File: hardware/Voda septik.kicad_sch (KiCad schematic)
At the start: 39 parts, among them J1 Screw_Terminal_01x09, J2 RS-485 elektroměr, J3 Display TM1637, J4 Display LCD I2C, U1 ESP32-DevKitC-30, U2 DC-DC 24V -> 5V, U4 MAX3485-modul

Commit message: Doladění průtoku a schematu.
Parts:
- removed R10: 22k, symbol Device:R
- removed R12: 10k, symbol Device:R
- added C6: 100p, symbol Device:C
- added C7: 1n, symbol Device:C
- C3: value 100n -> 15n
- D5: value ~ -> 1N4007; footprint (none) -> Diode_THT:D_DO-41_SOD81_P10.16mm_Horizontal
- R1: value 10k -> 2k2
- R11: value 10k -> 56R
- R2: value 10k -> 3k9
- R4: value 2k2 -> 2k7
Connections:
- net GND: now also C6.2, C7.2
- net průtok_MCU: now also R2.2, C7.1
- net temp_MCU: now also C6.1
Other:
- moved on the sheet: R2

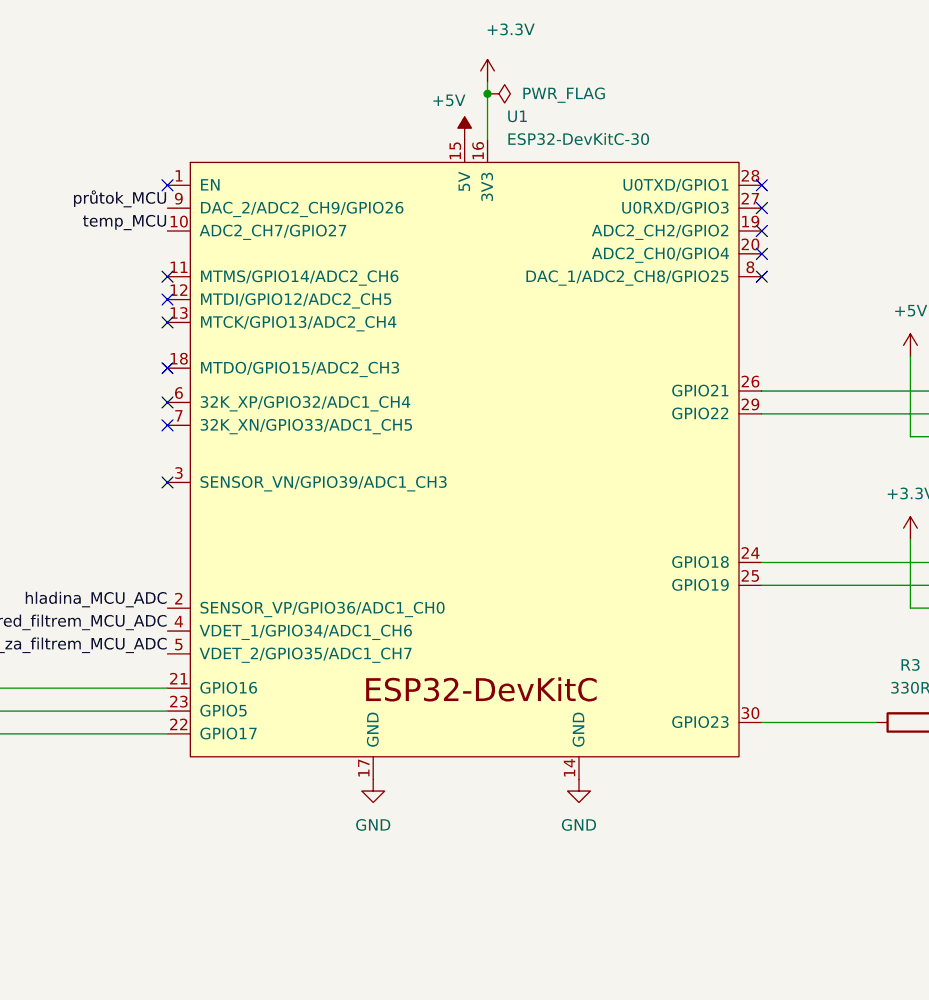
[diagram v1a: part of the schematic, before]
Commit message: Upravit schéma podle skutečnosti.
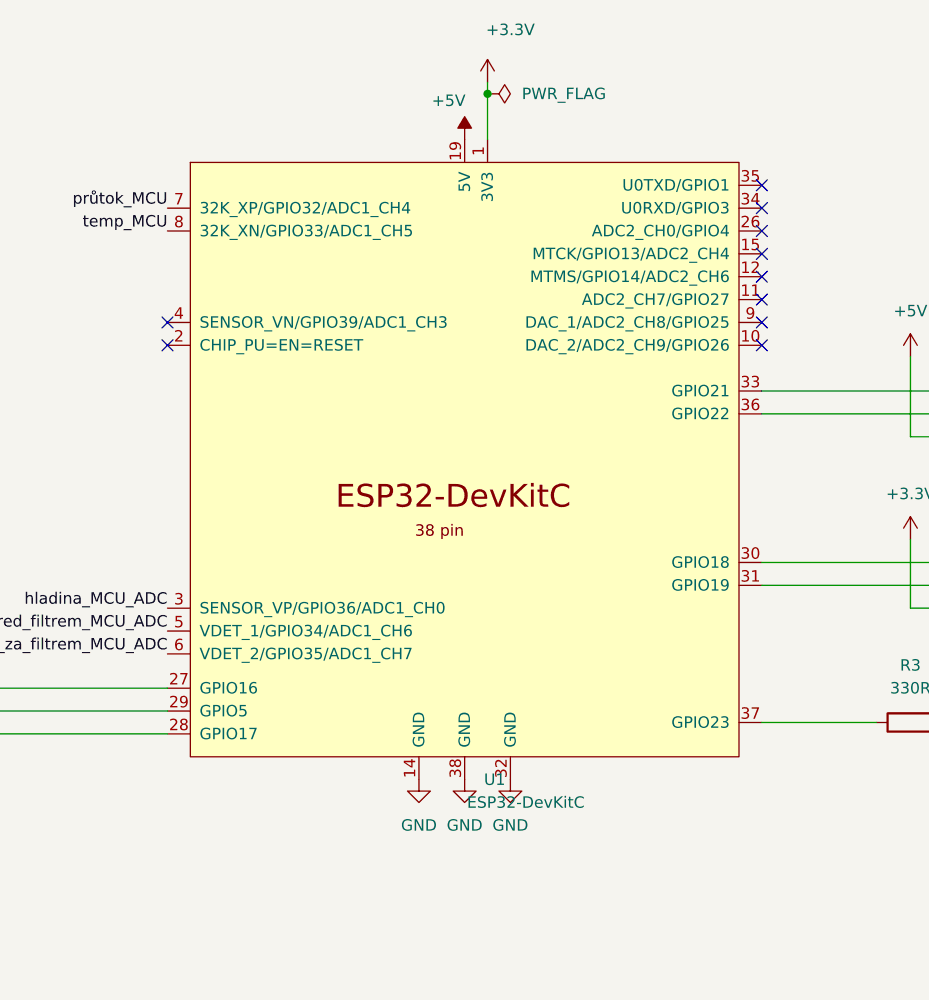
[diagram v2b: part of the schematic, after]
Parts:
- U1: value ESP32-DevKitC-30 -> ESP32-DevKitC; footprint martin:ESP32-DevKitC-30 -> PCM_Espressif:ESP32-DevKitC; symbol martin:ESP32-DevKitC-30 -> PCM_Espressif:ESP32-DevKitC
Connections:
- net +3.3V: now also U1.1 (3V3); no longer U1.16 (3V3)
- net +5V: now also U1.19 (5V); no longer U1.15 (5V)
- net GND: now also U1.32 (GND), U1.38 (GND); no longer U1.17 (GND)
- net hladina_MCU_ADC: now also U1.3 (SENSOR_VP/GPIO36/ADC1_CH0); no longer U1.2 (SENSOR_VP/GPIO36/ADC1_CH0)
- net průtok_MCU: now also U1.7 (32K_XP/GPIO32/ADC1_CH4); no longer U1.9 (DAC_2/ADC2_CH9/GPIO26)
- net temp_MCU: now also U1.8 (32K_XN/GPIO33/ADC1_CH5); no longer U1.10 (ADC2_CH7/GPIO27)
- net tlak_pred_filtrem_MCU_ADC: now also U1.5 (VDET_1/GPIO34/ADC1_CH6); no longer U1.4 (VDET_1/GPIO34/ADC1_CH6)
- net tlak_za_filtrem_MCU_ADC: now also U1.6 (VDET_2/GPIO35/ADC1_CH7); no longer U1.5 (VDET_2/GPIO35/ADC1_CH7)
- net at R3.1: now also U1.37 (GPIO23); no longer U1.30 (GPIO23)
- net at J3.3 (DIO): now also U1.31 (GPIO19); no longer U1.25 (GPIO19)
- net at J3.4 (CLK): now also U1.30 (GPIO18); no longer U1.24 (GPIO18)
- net at U4.1 (RXD): now also U1.27 (GPIO16); no longer U1.21 (GPIO16)
- net at U4.3 (EN): now also U1.29 (GPIO5); no longer U1.23 (GPIO5)
- net at U4.4 (TXD): now also U1.28 (GPIO17); no longer U1.22 (GPIO17)
- net at U1.26 (ADC2_CH0/GPIO4): no longer J4.4 (SCL)
- net at J4.3 (SDA): now also U1.36 (GPIO22); no longer U1.29 (GPIO22)
- new net: J4.4 (SCL), U1.33 (GPIO21)
- no-connect marks 13 -> 10
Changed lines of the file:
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@@
 	)
 	(no_connect
-		(at 165.1 40.64)
+		(at 231.14 45.72)
 	)
 	(no_connect
@@
 	)
 	(no_connect
-		(at 165.1 43.18)
+		(at 231.14 48.26)
 	)
 	(no_connect
-		(at 165.1 30.48)
+		(at 231.14 43.18)
 	)
 	(no_connect
@@
 	)
 	(no_connect
-		(at 165.1 57.15)
-	)
-	(no_connect
 		(at 231.14 30.48)
 	)
 	(no_connect
-		(at 165.1 54.61)
-	)
-	(no_connect
-		(at 165.1 63.5)
-	)
-	(no_connect
 		(at 231.14 40.64)
 	)
 	(no_connect
-		(at 165.1 50.8)
+		(at 165.1 48.26)
 	)
 	(wire
@@
 	(symbol
 		(lib_id "power:GND")
-		(at 210.82 96.52 0)
+		(at 203.2 96.52 0)
 		(unit 1)
 		(exclude_from_sim no)
@@
 		(fields_autoplaced yes)
 		(property "Reference" "#PWR021"
-			(at 210.82 102.87 0)
+			(at 203.2 102.87 0)
 			(effects
 				(font
@@
 		)
 		(property "Value" "GND"
-			(at 210.82 101.6 0)
+			(at 203.2 101.6 0)
 			(effects
 				(font
@@
 		)
 		(property "Footprint" ""
-			(at 210.82 96.52 0)
+			(at 203.2 96.52 0)
 			(effects
 				(font
@@
 		)
 		(property "Datasheet" ""
-			(at 210.82 96.52 0)
+			(at 203.2 96.52 0)
 			(effects
 				(font
@@
 		)
 		(property "Description" "Power symbol creates a global label with name \"GND\" , ground"
-			(at 210.82 96.52 0)
+			(at 203.2 96.52 0)
 			(effects
 				(font
@@
 	)
 	(symbol
-		(lib_id "martin:ESP32-DevKitC-30")
+		(lib_id "PCM_Espressif:ESP32-DevKitC")
 		(at 198.12 60.96 0)
 		(unit 1)
@@
 		(on_board yes)
 		(dnp no)
-		(fields_autoplaced yes)
 		(property "Reference" "U1"
-			(at 202.8033 22.86 0)
+			(at 200.2633 96.52 0)
 			(effects
 				(font
@@
 			)
 		)
-		(property "Value" "ESP32-DevKitC-30"
-			(at 202.8033 25.4 0)
+		(property "Value" "ESP32-DevKitC"
+			(at 198.374 99.06 0)
 			(effects
 				(font
@@
 			)
 		)
-		(property "Footprint" "martin:ESP32-DevKitC-30"
+		(property "Footprint" "PCM_Espressif:ESP32-DevKitC"
 			(at 198.12 104.14 0)
 			(effects
@@
 		(pin "22"
 		)
+		(pin "32"
+		)
+		(pin "38"
+		)
+		(pin "35"
+		)
+		(pin "34"
+		)
+		(pin "31"
+		)
+		(pin "33"
+		)
+		(pin "36"
+		)
+		(pin "37"
+		)
 		(instances
 			(project ""
@@
 	)
 	(symbol
+		(lib_id "power:GND")
+		(at 198.12 96.52 0)
+		(unit 1)
+		(exclude_from_sim no)
+		(in_bom yes)
+		(on_board yes)
+		(dnp no)
+		(fields_autoplaced yes)
+		(property "Reference" "#PWR026"
+			(at 198.12 102.87 0)
+			(effects
+				(font
+					(size 1.27 1.27)
+				)
+				(hide yes)
+			)
+		)
+		(property "Value" "GND"
+			(at 198.12 101.6 0)
+			(effects
+				(font
+					(size 1.27 1.27)
+				)
+			)
+		)
+		(property "Footprint" ""
+			(at 198.12 96.52 0)
+			(effects
+				(font
+					(size 1.27 1.27)
+				)
+				(hide yes)
+			)
+		)
+		(property "Datasheet" ""
+			(at 198.12 96.52 0)
+			(effects
+				(font
+					(size 1.27 1.27)
+				)
+				(hide yes)
+			)
+		)
+		(property "Description" "Power symbol creates a global label with name \"GND\" , ground"
+			(at 198.12 96.52 0)
+			(effects
+				(font
+					(size 1.27 1.27)
+				)
+				(hide yes)
+			)
+		)
+		(pin "1"
+		)
+		(instances
+			(project "Voda septik"
+				(path "/cbe5bfb0-423d-4741-99d1-40044a77c19e"
+					(reference "#PWR026")
+					(unit 1)
+				)
+			)
+		)
+	)
+	(symbol
 		(lib_id "martin:DC_DC_LM2596_HW411")
 		(at 57.15 27.94 0)
@@
 	(symbol
 		(lib_id "power:GND")
-		(at 187.96 96.52 0)
+		(at 193.04 96.52 0)
 		(unit 1)
 		(exclude_from_sim no)
@@
 		(fields_autoplaced yes)
 		(property "Reference" "#PWR020"
-			(at 187.96 102.87 0)
+			(at 193.04 102.87 0)
 			(effects
 				(font
@@
 		)
 		(property "Value" "GND"
-			(at 187.96 101.6 0)
+			(at 193.04 101.6 0)
 			(effects
 				(font
@@
 		)
 		(property "Footprint" ""
-			(at 187.96 96.52 0)
+			(at 193.04 96.52 0)
 			(effects
 				(font
@@
 		)
 		(property "Datasheet" ""
-			(at 187.96 96.52 0)
+			(at 193.04 96.52 0)
 			(effects
 				(font
@@
 		)
 		(property "Description" "Power symbol creates a global label with name \"GND\" , ground"
-			(at 187.96 96.52 0)
+			(at 193.04 96.52 0)
 			(effects
 				(font

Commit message: Úprava schématu, asi popisky.
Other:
- note added: "hladina"
- note added: "průtok"
- note added: "svítí při chybě senzoru"
- note added: "teplota voda"
- note added: "teplota vzduch"
- note added: "tlak před filtrem"
- note added: "tlak za filtrem"

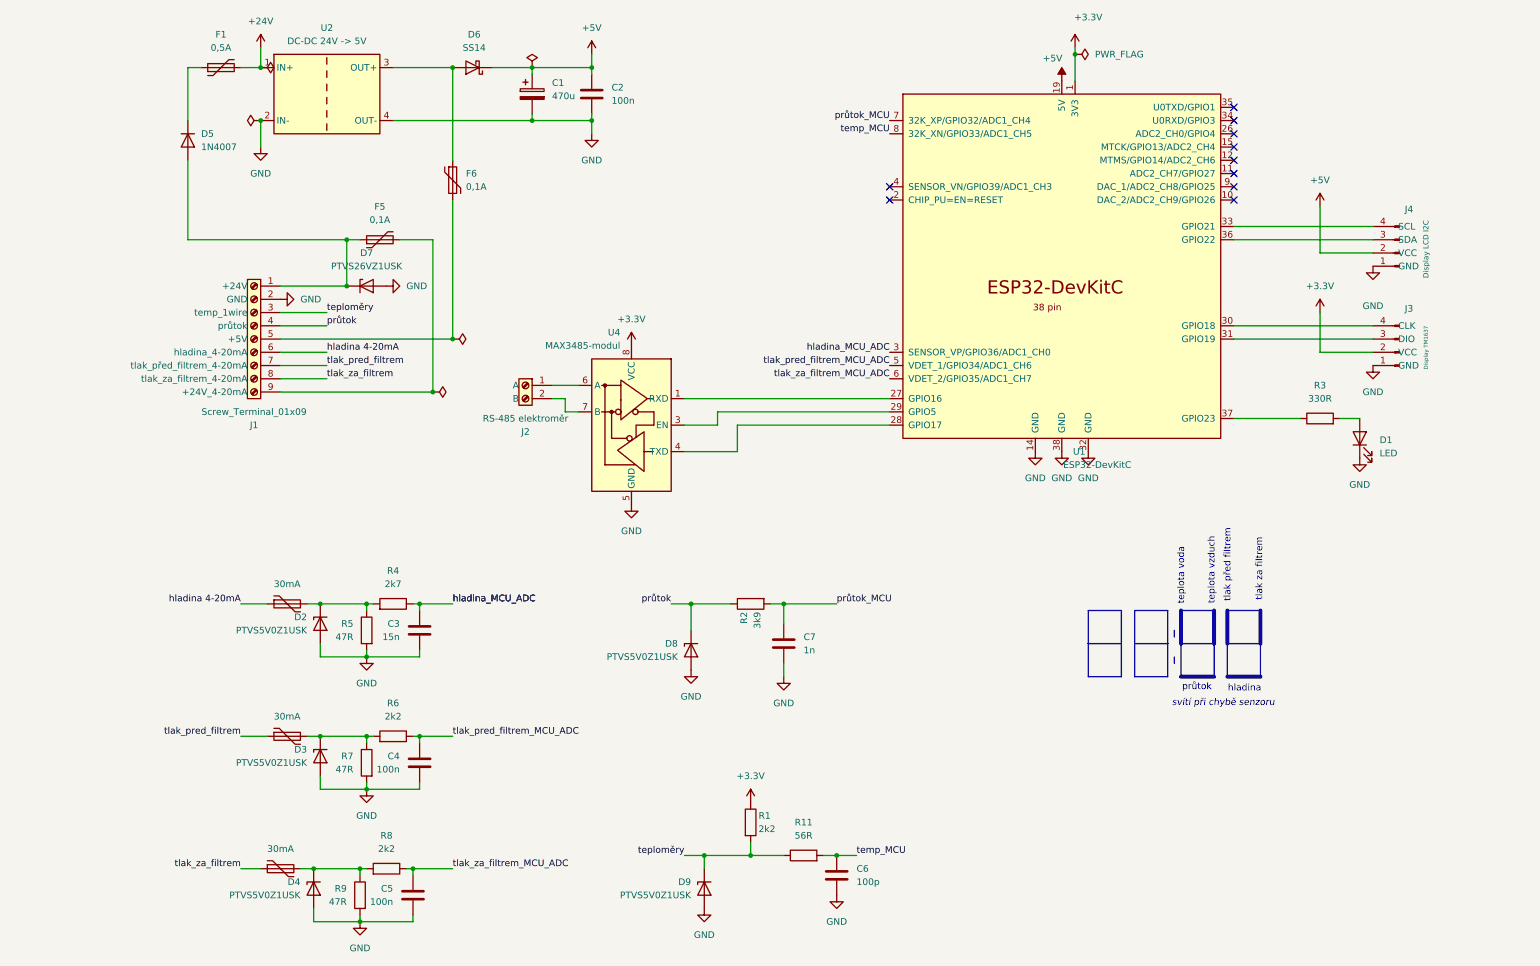
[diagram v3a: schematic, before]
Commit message: Úprava schématu
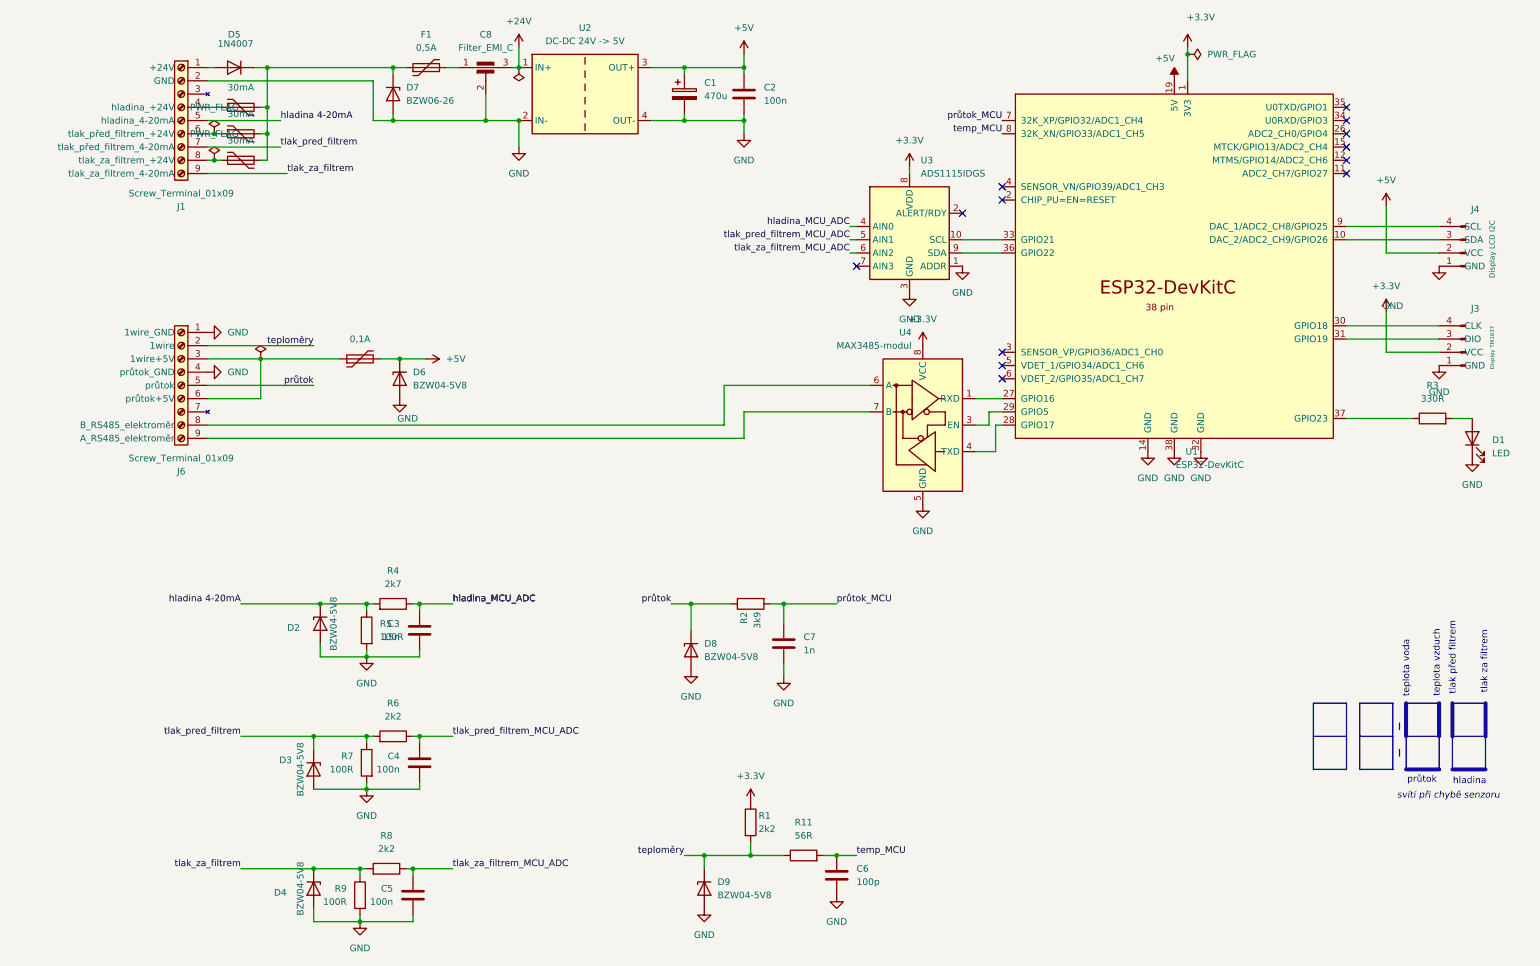
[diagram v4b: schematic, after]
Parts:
- removed D3, D4: PTVS5V0Z1USK, Diode_SMD:Nexperia_DSN1608-2_1.6x0.8mm, symbol Diode:PTVS5V0Z1USK
- removed D6: SS14, symbol Device:D_Schottky
- removed F6: 0,1A, symbol Device:Polyfuse
- removed J2: RS-485 elektroměr, TerminalBlock_RND:TerminalBlock_RND_205-00001_1x02_P5.00mm_Horizontal, symbol Connector:Screw_Terminal_01x02
- added C8: Filter_EMI_C, symbol Device:Filter_EMI_C
- added D3, D4, D6: BZW04-5V8, Diode_THT:D_DO-15_P10.16mm_Horizontal, symbol martin:BZW04-5V8
- added J6: Screw_Terminal_01x09, TerminalBlock_Phoenix:TerminalBlock_Phoenix_MKDS-1,5-9_1x09_P5.00mm_Horizontal, symbol Connector:Screw_Terminal_01x09
- added U3: ADS1115IDGS, Package_SO:TSSOP-10_3x3mm_P0.5mm, symbol Analog_ADC:ADS1115IDGS
- D2, D8, D9: value PTVS5V0Z1USK -> BZW04-5V8; footprint Diode_SMD:Nexperia_DSN1608-2_1.6x0.8mm -> Diode_THT:D_DO-15_P10.16mm_Horizontal; symbol Diode:PTVS5V0Z1USK -> martin:BZW04-5V8
- D7: value PTVS26VZ1USK -> BZW06-26; footprint Diode_SMD:Nexperia_DSN1608-2_1.6x0.8mm -> Diode_THT:D_DO-15_P10.16mm_Horizontal; symbol Diode:PTVS26VZ1USK -> martin:BZW06-26
- J1: footprint TerminalBlock_Phoenix:TerminalBlock_Phoenix_MKDS-1,5-9_1x09_P5.00mm_Horizontal -> TerminalBlock:TerminalBlock_Xinya_XY308-2.54-9P_1x09_P2.54mm_Horizontal
- R5, R7, R9: value 47R -> 100R
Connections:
- net +24V: now also C8.3; no longer F1.2
- net +3.3V: now also U3.8 (VDD)
- net +5V: now also F5.2, U2.3 (OUT+), D6.1 (K)
- net GND: now also C8.2, D3.2 (A), D4.2 (A), D6.2 (A), J6.1 (1wire_GND), J6.4 (průtok_GND), U3.1 (ADDR), U3.3 (GND)
- net hladina 4-20mA: now also D2.1 (K), J1.5 (hladina_4-20mA), R4.2, R5.1; no longer F2.1, J1.6 (hladina_4-20mA)
- net hladina_MCU_ADC: now also U3.4 (AIN0); no longer U1.3 (SENSOR_VP/GPIO36/ADC1_CH0)
- net průtok: now also J6.5 (průtok); no longer J1.4 (průtok)
- net teploměry: now also J6.2 (1wire); no longer J1.3 (temp_1wire)
- net tlak_pred_filtrem: now also R6.2, R7.1, D3.1 (K); no longer F3.1
- net tlak_pred_filtrem_MCU_ADC: now also U3.5 (AIN1); no longer U1.5 (VDET_1/GPIO34/ADC1_CH6)
- net tlak_za_filtrem: now also J1.9 (tlak_za_filtrem_4-20mA), R8.2, R9.1, D4.1 (K); no longer F4.1, J1.8 (tlak_za_filtrem_4-20mA)
- net tlak_za_filtrem_MCU_ADC: now also U3.6 (AIN2); no longer U1.6 (VDET_2/GPIO35/ADC1_CH7)
- net at D5.1 (K), F1.1: now also D7.1 (K), F2.2, F3.2, F4.2
- net at U4.6 (A): now also J6.8 (B_RS485_elektroměr)
- net at U4.7 (B): now also J6.9 (A_RS485_elektroměr)
- net at U1.10 (DAC_2/ADC2_CH9/GPIO26): now also J4.3 (SDA)
- net at U1.33 (GPIO21): now also U3.10 (SCL); no longer J4.4 (SCL)
- net at U1.36 (GPIO22): now also U3.9 (SDA); no longer J4.3 (SDA)
- net at U1.9 (DAC_1/ADC2_CH8/GPIO25): now also J4.4 (SCL)
- net at D5.2 (A), J1.1 (+24V): no longer D7.1 (K), F5.1
- new net: C8.1, F1.2
- new net: F3.1, J1.6 (tlak_před_filtrem_+24V)
- new net: F4.1, J1.8 (tlak_za_filtrem_+24V)
- new net: F2.1, J1.4 (hladina_+24V)
- new net: F5.1, J6.3 (1wire+5V), J6.6 (průtok+5V)
- no-connect marks 10 -> 13
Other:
- moved on the sheet: C1, C2, D1, D5, D7, F1, J3, J4, R3, U1, U2, U4
